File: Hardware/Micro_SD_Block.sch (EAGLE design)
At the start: 17 parts, among them U1 USD-SOCKETNEW, U2 EDISON_CONNECTOR_FULLMOUNTING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, U3 EDISON_CONNECTOR_FULLHEADER

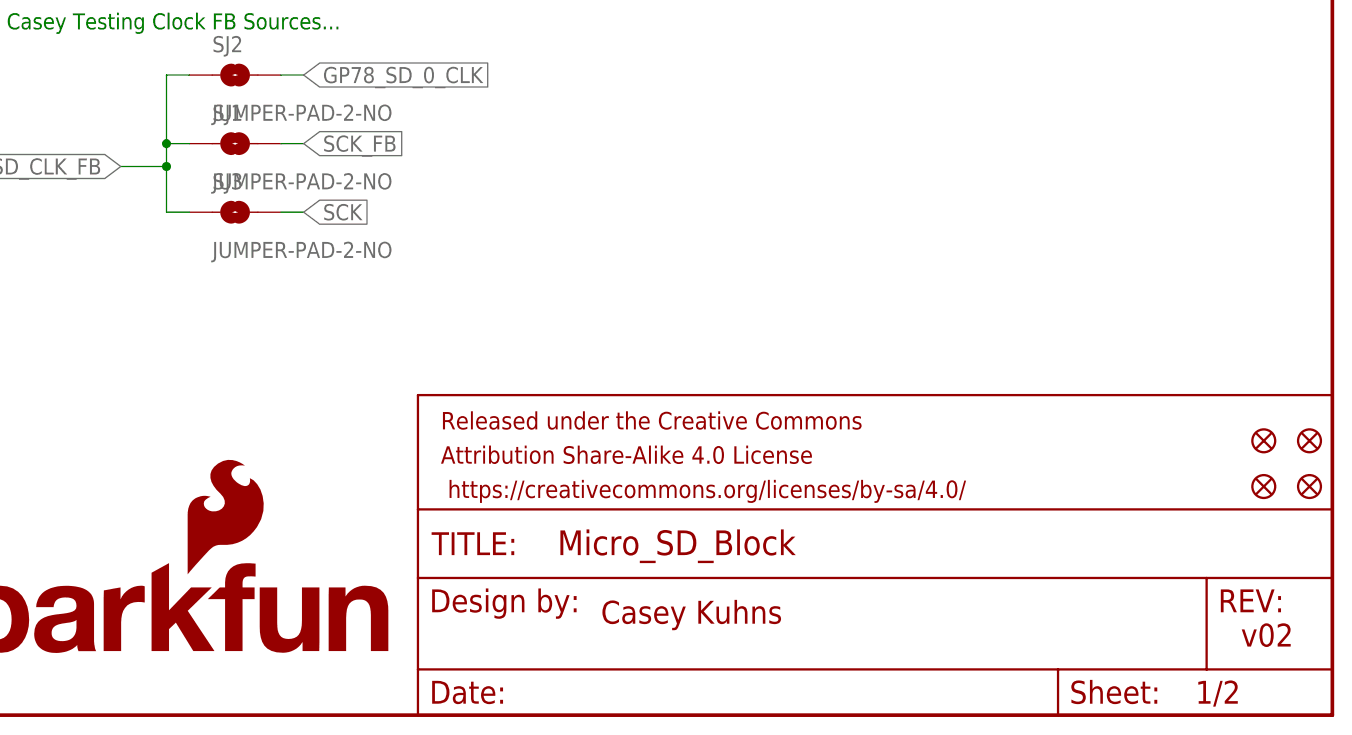
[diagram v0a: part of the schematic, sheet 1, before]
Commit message: removed thermals on connectors updated connector to new foot print updated version number corrected silk positions
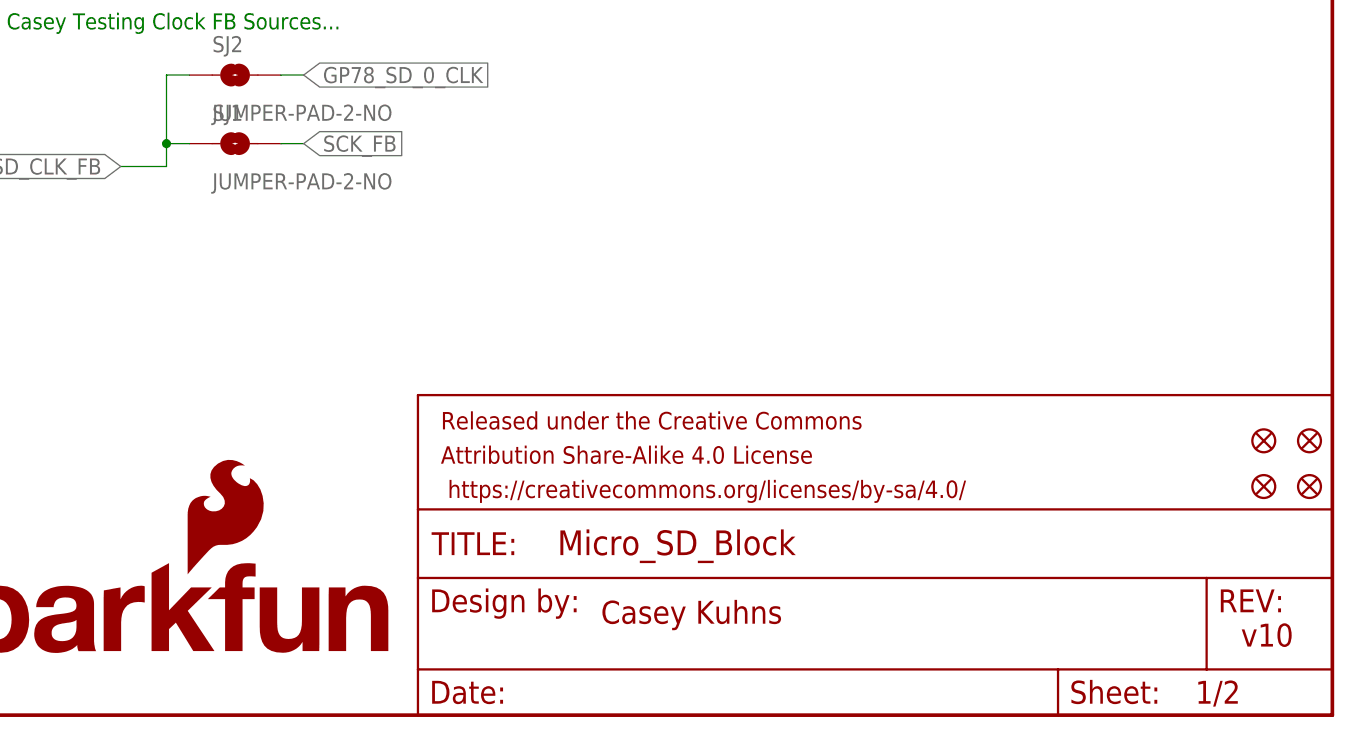
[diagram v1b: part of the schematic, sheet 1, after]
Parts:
- removed SJ3: JUMPER-PAD-2-NO, SparkFun-Passives:JUMPER-PAD-2-NO
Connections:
- net GP84_SD_CLK_FB: no longer SJ3.1
- net SCK: no longer SJ3.2
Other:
- note added: "v10"
- note removed: "v02"
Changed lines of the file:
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@@
 <?xml version="1.0" encoding="utf-8"?>
 <!DOCTYPE eagle SYSTEM "eagle.dtd">
-<eagle version="6.5.0">
+<eagle version="6.6.0">
 <drawing>
 <settings>
@@
 <part name="SJ2" library="SparkFun-Passives" deviceset="JUMPER-PAD-2-NO" device=""/>
 <part name="SJ1" library="SparkFun-Passives" deviceset="JUMPER-PAD-2-NO" device=""/>
-<part name="SJ3" library="SparkFun-Passives" deviceset="JUMPER-PAD-2-NO" device=""/>
 </parts>
 <sheets>
@@
 <plain>
 <text x="167.64" y="10.16" size="2.54" layer="94">Casey Kuhns</text>
-<text x="238.76" y="7.62" size="2.54" layer="94">v02</text>
+<text x="238.76" y="7.62" size="2.54" layer="94">v10</text>
 <text x="93.98" y="76.2" size="1.778" layer="91">This is Casey Testing Clock FB Sources...</text>
 </plain>
@@
 <instance part="SJ2" gate="G$1" x="127" y="71.12"/>
 <instance part="SJ1" gate="G$1" x="127" y="63.5"/>
-<instance part="SJ3" gate="G$1" x="127" y="55.88"/>
 </instances>
 <busses>
@@
 <junction x="142.24" y="116.84"/>
 </segment>
-<segment>
-<pinref part="SJ3" gate="G$1" pin="2"/>
-<wire x1="132.08" y1="55.88" x2="134.62" y2="55.88" width="0.1524" layer="91"/>
-<label x="134.62" y="55.88" size="1.778" layer="95" xref="yes"/>
-</segment>
 </net>
 <net name="N$5" class="0">
@@
 <wire x1="119.38" y1="63.5" x2="121.92" y2="63.5" width="0.1524" layer="91"/>
 <wire x1="119.38" y1="63.5" x2="119.38" y2="60.96" width="0.1524" layer="91"/>
-<pinref part="SJ3" gate="G$1" pin="1"/>
-<wire x1="119.38" y1="60.96" x2="119.38" y2="55.88" width="0.1524" layer="91"/>
-<wire x1="119.38" y1="55.88" x2="121.92" y2="55.88" width="0.1524" layer="91"/>
 <wire x1="119.38" y1="60.96" x2="114.3" y2="60.96" width="0.1524" layer="91"/>
-<junction x="119.38" y="60.96"/>
 <label x="114.3" y="60.96" size="1.778" layer="95" rot="R180" xref="yes"/>
 <junction x="119.38" y="63.5"/>

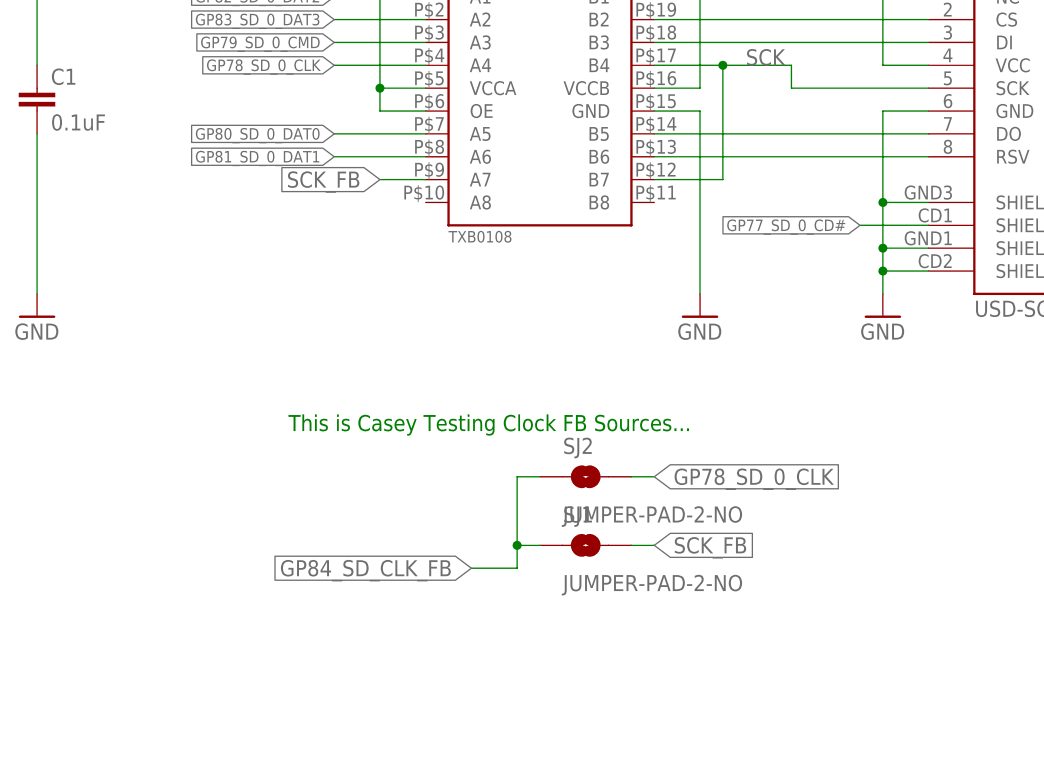
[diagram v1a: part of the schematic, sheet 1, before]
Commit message: modified traces to eliminate bridging.  Selected FB circuit to use in production.
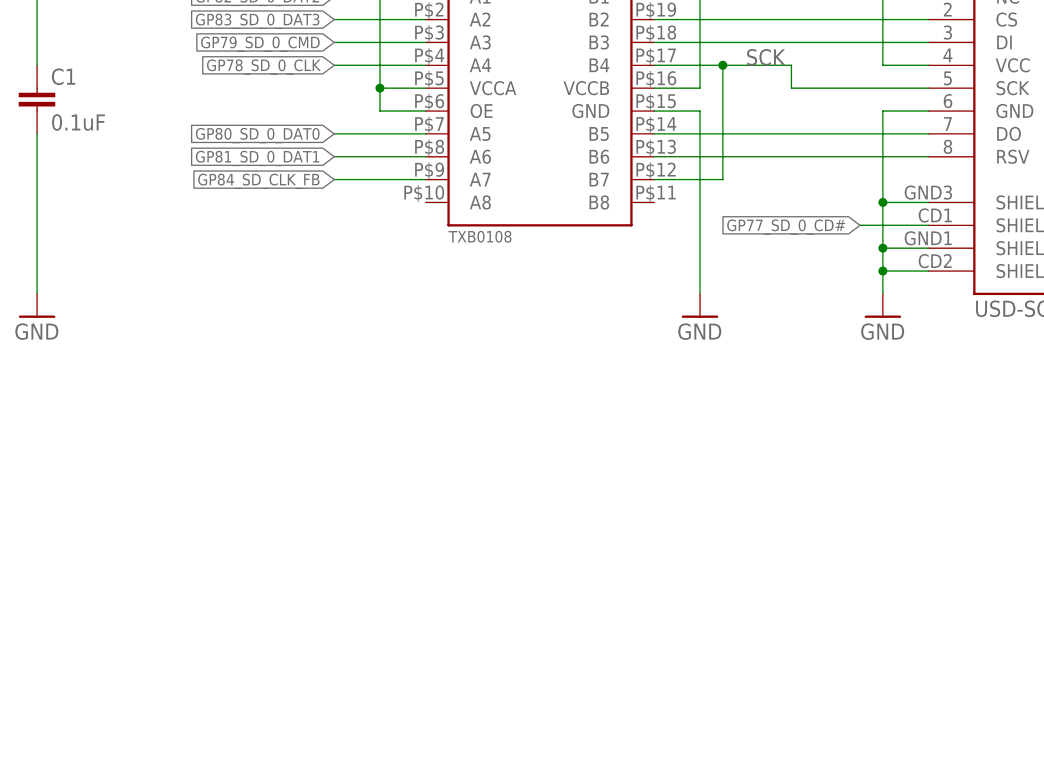
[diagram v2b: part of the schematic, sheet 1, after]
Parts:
- removed SJ1, SJ2: JUMPER-PAD-2-NO, SparkFun-Passives:JUMPER-PAD-2-NO
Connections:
- removed net SCK_FB: SJ1.2, U$1.A7
- net GP78_SD_0_CLK: no longer SJ2.2
- net GP84_SD_CLK_FB: now also U$1.A7; no longer SJ1.1, SJ2.1
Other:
- note removed: "This is Casey Testing Clock FB Sources..."
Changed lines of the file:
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@@
 <part name="GND7" library="SparkFun-Aesthetics" deviceset="GND" device=""/>
 <part name="SUPPLY5" library="SparkFun-Aesthetics" deviceset="3.3V" device=""/>
-<part name="SJ2" library="SparkFun-Passives" deviceset="JUMPER-PAD-2-NO" device=""/>
-<part name="SJ1" library="SparkFun-Passives" deviceset="JUMPER-PAD-2-NO" device=""/>
 </parts>
 <sheets>
@@
 <text x="167.64" y="10.16" size="2.54" layer="94">Casey Kuhns</text>
 <text x="238.76" y="7.62" size="2.54" layer="94">v10</text>
-<text x="93.98" y="76.2" size="1.778" layer="91">This is Casey Testing Clock FB Sources...</text>
 </plain>
 <instances>
@@
 <instance part="GND7" gate="1" x="198.12" y="88.9"/>
 <instance part="SUPPLY5" gate="G$1" x="198.12" y="132.08"/>
-<instance part="SJ2" gate="G$1" x="127" y="71.12"/>
-<instance part="SJ1" gate="G$1" x="127" y="63.5"/>
 </instances>
 <busses>
@@
 <pinref part="U$1" gate="G$1" pin="A4"/>
 </segment>
-<segment>
-<pinref part="SJ2" gate="G$1" pin="2"/>
-<wire x1="132.08" y1="71.12" x2="134.62" y2="71.12" width="0.1524" layer="91"/>
-<label x="134.62" y="71.12" size="1.778" layer="95" xref="yes"/>
-</segment>
 </net>
 <net name="GP77_SD_0_CD#" class="0">
@@
 <net name="GP84_SD_CLK_FB" class="0">
 <segment>
-<pinref part="SJ2" gate="G$1" pin="1"/>
-<wire x1="121.92" y1="71.12" x2="119.38" y2="71.12" width="0.1524" layer="91"/>
-<wire x1="119.38" y1="71.12" x2="119.38" y2="63.5" width="0.1524" layer="91"/>
-<pinref part="SJ1" gate="G$1" pin="1"/>
-<wire x1="119.38" y1="63.5" x2="121.92" y2="63.5" width="0.1524" layer="91"/>
-<wire x1="119.38" y1="63.5" x2="119.38" y2="60.96" width="0.1524" layer="91"/>
-<wire x1="119.38" y1="60.96" x2="114.3" y2="60.96" width="0.1524" layer="91"/>
-<label x="114.3" y="60.96" size="1.778" layer="95" rot="R180" xref="yes"/>
-<junction x="119.38" y="63.5"/>
-</segment>
-</net>
-<net name="SCK_FB" class="0">
-<segment>
+<wire x1="109.22" y1="104.14" x2="99.06" y2="104.14" width="0.1524" layer="91"/>
+<label x="99.06" y="104.14" size="1.27" layer="95" rot="R180" xref="yes"/>
 <pinref part="U$1" gate="G$1" pin="A7"/>
-<wire x1="109.22" y1="104.14" x2="104.14" y2="104.14" width="0.1524" layer="91"/>
-<label x="104.14" y="104.14" size="1.778" layer="95" rot="R180" xref="yes"/>
-</segment>
-<segment>
-<pinref part="SJ1" gate="G$1" pin="2"/>
-<wire x1="132.08" y1="63.5" x2="134.62" y2="63.5" width="0.1524" layer="91"/>
-<label x="134.62" y="63.5" size="1.778" layer="95" xref="yes"/>
-</segment>
-</net>
+</segment>
+</net>

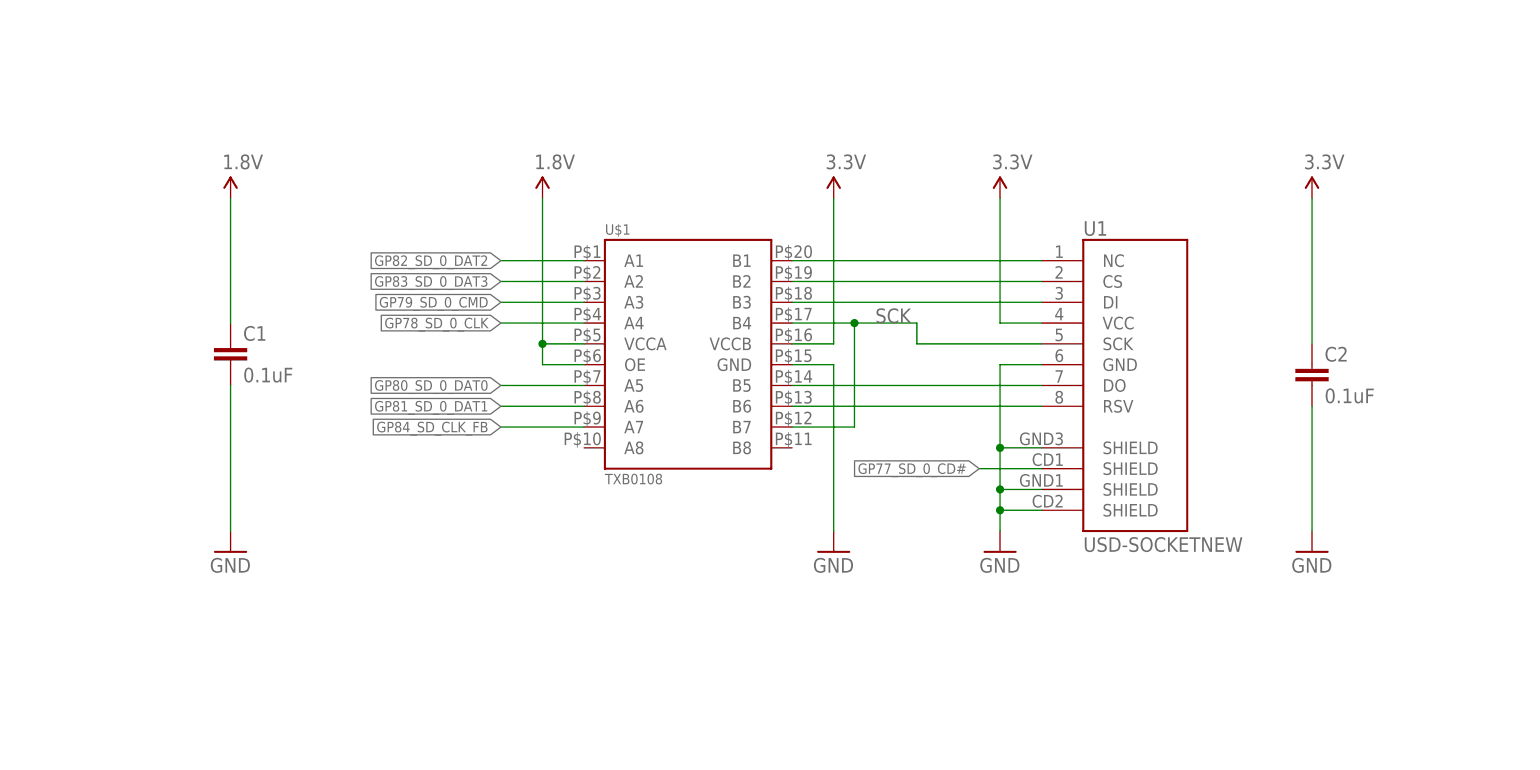
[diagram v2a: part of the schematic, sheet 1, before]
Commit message: Moved 3.3v bus out from under highspeed lines updated edison connector footprint to remove jumpers removed jumpers from txb0108
TODO: Remove P$#'s from txb0108 in library
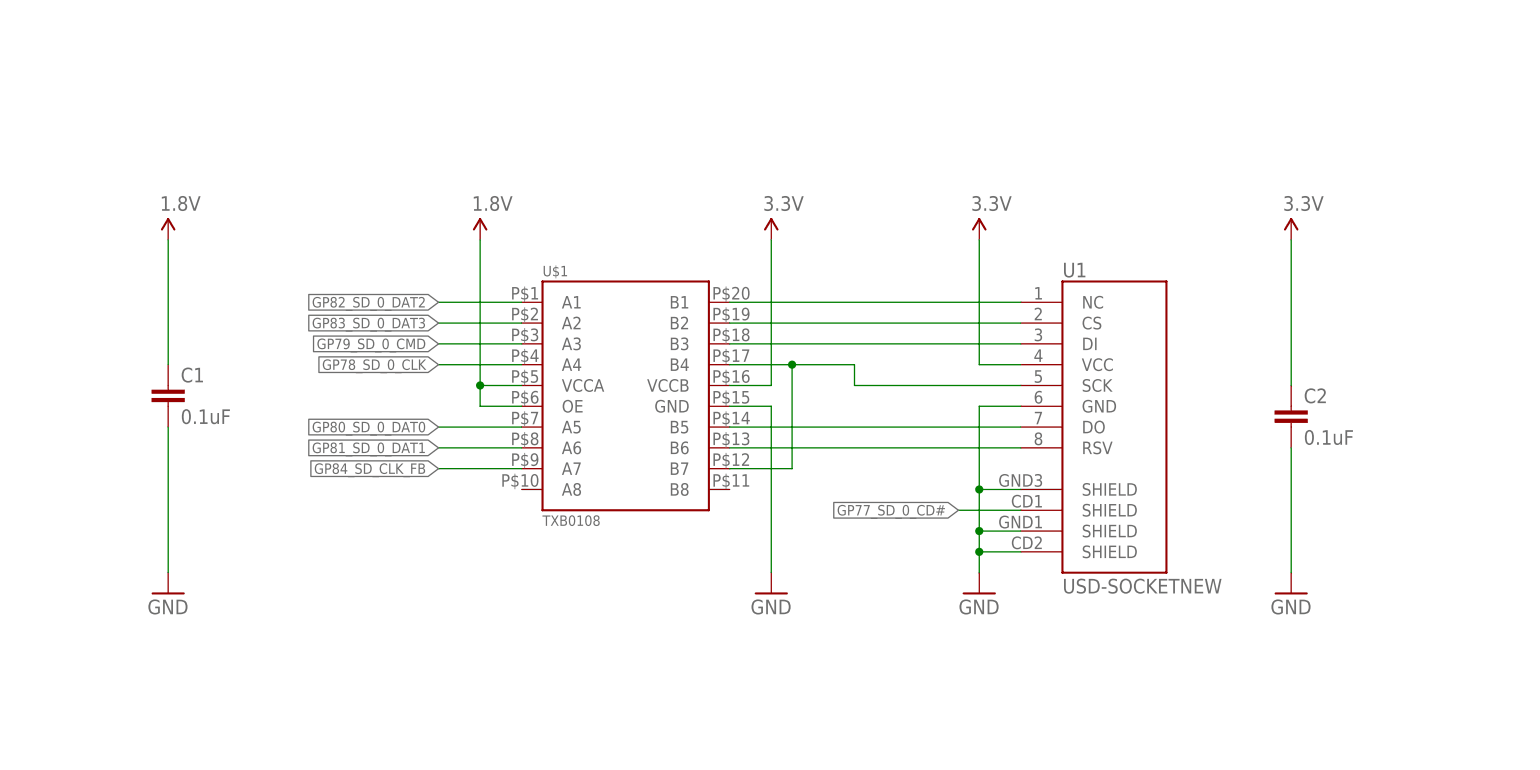
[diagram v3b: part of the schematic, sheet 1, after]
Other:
- moved on the sheet: C1, C2, U$1, U1
